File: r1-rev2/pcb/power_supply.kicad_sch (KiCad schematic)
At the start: 25 parts, among them J1 GT-BTP30003-xxxA-16A, Q1 AO3401A, U1 LM66100DCK, U2 TPS62A01DRLR, U3 TPS62A01DRLR, U4 TP4057, U5 XC6206P33xMR

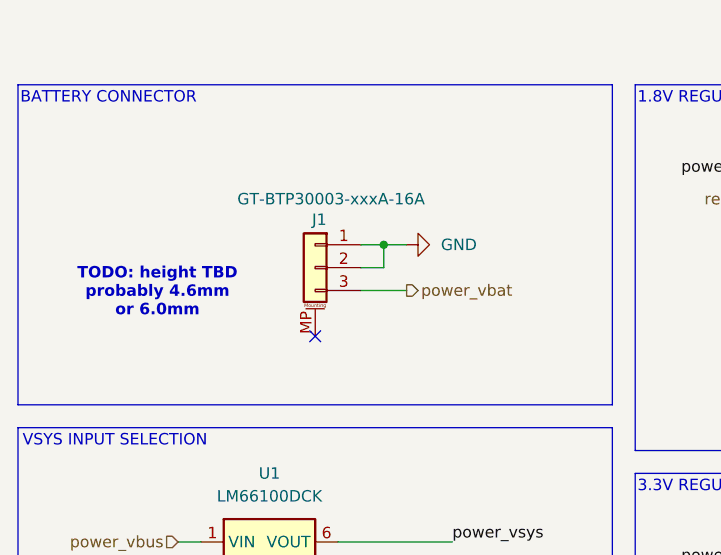
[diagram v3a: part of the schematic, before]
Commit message: R1-Rev2: finish STM32 pin assignment and fix ERC issues
- Expanded LCD bus from 8 to 16 pins so it can be accessed by DMA2D.
- Added RDX pin to LCD bus to allow read access
- Added UART console port for easier access to debug logging
- Shorted USB HS and FS PHYs for DFU mode support
- Connected all GPIOs and peripheral pins
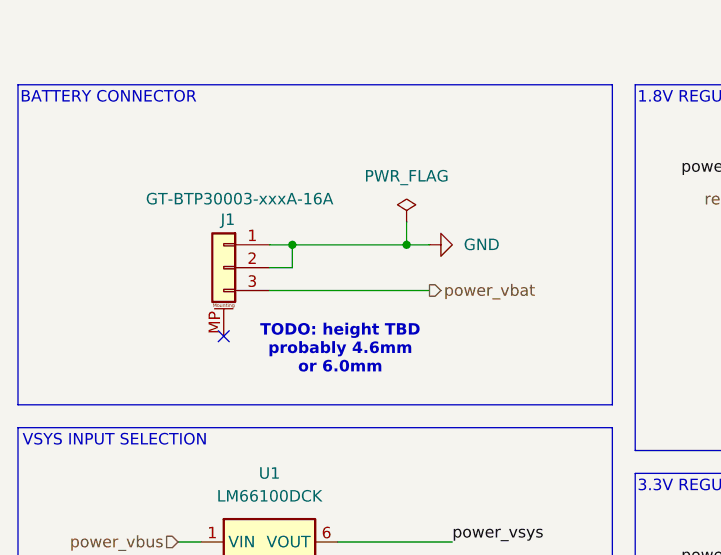
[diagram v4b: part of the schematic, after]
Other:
- moved on the sheet: J1
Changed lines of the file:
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@@
 	(text "TODO: height TBD\nprobably 4.6mm\nor 6.0mm"
 		(exclude_from_sim no)
-		(at 43.434 63.754 0)
+		(at 63.754 70.104 0)
 		(effects
 			(font
@@
 	)
 	(junction
+		(at 71.12 58.42)
+		(diameter 0)
+		(color 0 0 0 0)
+	)
+	(junction
 		(at 147.32 114.3)
 		(diameter 0)
@@
 	)
 	(junction
-		(at 68.58 58.42)
+		(at 58.42 58.42)
 		(diameter 0)
 		(color 0 0 0 0)
@@
 	)
 	(no_connect
-		(at 60.96 68.58)
+		(at 50.8 68.58)
 	)
 	(wire
@@
 	(wire
 		(pts
+			(xy 71.12 55.88) (xy 71.12 58.42)
+		)
+		(stroke
+			(width 0)
+			(type default)
+		)
+	)
+	(wire
+		(pts
 			(xy 129.54 114.3) (xy 129.54 116.84)
 		)
@@
 	(wire
 		(pts
-			(xy 66.04 63.5) (xy 71.12 63.5)
+			(xy 55.88 63.5) (xy 73.66 63.5)
 		)
 		(stroke
@@
 	(wire
 		(pts
-			(xy 66.04 60.96) (xy 68.58 60.96)
+			(xy 55.88 60.96) (xy 58.42 60.96)
 		)
 		(stroke
@@
 	(wire
 		(pts
-			(xy 68.58 58.42) (xy 71.12 58.42)
+			(xy 58.42 58.42) (xy 71.12 58.42)
 		)
 		(stroke
@@
 	(wire
 		(pts
+			(xy 71.12 58.42) (xy 73.66 58.42)
+		)
+		(stroke
+			(width 0)
+			(type default)
+		)
+	)
+	(wire
+		(pts
 			(xy 149.86 60.96) (xy 149.86 63.5)
 		)
@@
 	(wire
 		(pts
-			(xy 66.04 58.42) (xy 68.58 58.42)
+			(xy 55.88 58.42) (xy 58.42 58.42)
 		)
 		(stroke
@@
 	(wire
 		(pts
-			(xy 68.58 58.42) (xy 68.58 60.96)
+			(xy 58.42 58.42) (xy 58.42 60.96)
 		)
 		(stroke
@@
 	(hierarchical_label "power_vbat"
 		(shape output)
-		(at 71.12 63.5 0)
+		(at 73.66 63.5 0)
 		(effects
 			(font
@@
 	(symbol
 		(lib_id "echoplayer:GT-BTP30003")
-		(at 60.96 60.96 0)
+		(at 50.8 60.96 0)
 		(mirror y)
 		(unit 1)
@@
 		(dnp no)
 		(property "Reference" "J1"
-			(at 62.23 55.626 0)
+			(at 52.07 55.626 0)
 			(effects
 				(font
@@
 		)
 		(property "Value" "GT-BTP30003-xxxA-16A"
-			(at 73.152 53.34 0)
+			(at 62.992 53.34 0)
 			(effects
 				(font
@@
 		)
 		(property "Footprint" "echoplayer:Conn_GT-BTP30003-xxxxA-016A"
-			(at 60.96 60.96 0)
+			(at 50.8 60.96 0)
 			(effects
 				(font
@@
 		)
 		(property "Datasheet" "https://www.lcsc.com/datasheet/lcsc_datasheet_2409091552_G-Switch-GT-BTP30003-0460A-016A_C41378737.pdf"
-			(at 60.96 60.96 0)
+			(at 50.8 60.96 0)
 			(effects
 				(font
@@
 		)
 		(property "Description" "3-pin blade/shrapnel battery connector, SMD, vertical mount with mounting pin"
-			(at 60.96 60.96 0)
+			(at 50.8 60.96 0)
 			(effects
 				(font
@@
 	(symbol
 		(lib_id "power:GND")
-		(at 71.12 58.42 90)
+		(at 73.66 58.42 90)
 		(unit 1)
 		(exclude_from_sim no)
@@
 		(fields_autoplaced yes)
 		(property "Reference" "#PWR011"
-			(at 77.47 58.42 0)
+			(at 80.01 58.42 0)
 			(effects
 				(font
@@
 		)
 		(property "Value" "GND"
-			(at 74.93 58.4199 90)
+			(at 77.47 58.4199 90)
 			(effects
 				(font
@@
 		)
 		(property "Footprint" ""
-			(at 71.12 58.42 0)
+			(at 73.66 58.42 0)
 			(effects
 				(font
@@
 		)
 		(property "Datasheet" ""
-			(at 71.12 58.42 0)
+			(at 73.66 58.42 0)
 			(effects
 				(font
@@
 		)
 		(property "Description" "Power symbol creates a global label with name \"GND\" , ground"
-			(at 71.12 58.42 0)
+			(at 73.66 58.42 0)
 			(effects
 				(font
@@
 					(unit 1)
 				)
+			)
+		)
+	)
+	(symbol
+		(lib_id "power:PWR_FLAG")
+		(at 71.12 55.88 0)
+		(unit 1)
+		(exclude_from_sim no)
+		(in_bom yes)
+		(on_board yes)
+		(dnp no)
+		(fields_autoplaced yes)
+		(property "Reference" "#FLG010"
+			(at 71.12 53.975 0)
+			(effects
+				(font
+					(size 1.27 1.27)
+				)
+				(hide yes)
+			)
+		)
+		(property "Value" "PWR_FLAG"
+			(at 71.12 50.8 0)
+			(effects
+				(font
+					(size 1.27 1.27)
+				)
+			)
+		)
+		(property "Footprint" ""
+			(at 71.12 55.88 0)
+			(effects
+				(font
+					(size 1.27 1.27)
+				)
+				(hide yes)
+			)
+		)
+		(property "Datasheet" "~"
+			(at 71.12 55.88 0)
+			(effects
+				(font
+					(size 1.27 1.27)
+				)
+				(hide yes)
+			)
+		)
+		(property "Description" "Special symbol for telling ERC where power comes from"
+			(at 71.12 55.88 0)
+			(effects
+				(font
+					(size 1.27 1.27)
+				)
+				(hide yes)
+			)
+		)
+		(pin "1"
+		)
+		(instances
+			(project "echo-r1"
+				(path "/aa241847-30f4-429d-a148-6a6e39ba98e0/48d39f5c-11a4-46cd-927a-56a9c6ae42fa"
+					(reference "#FLG010")
+					(unit 1)
+				)

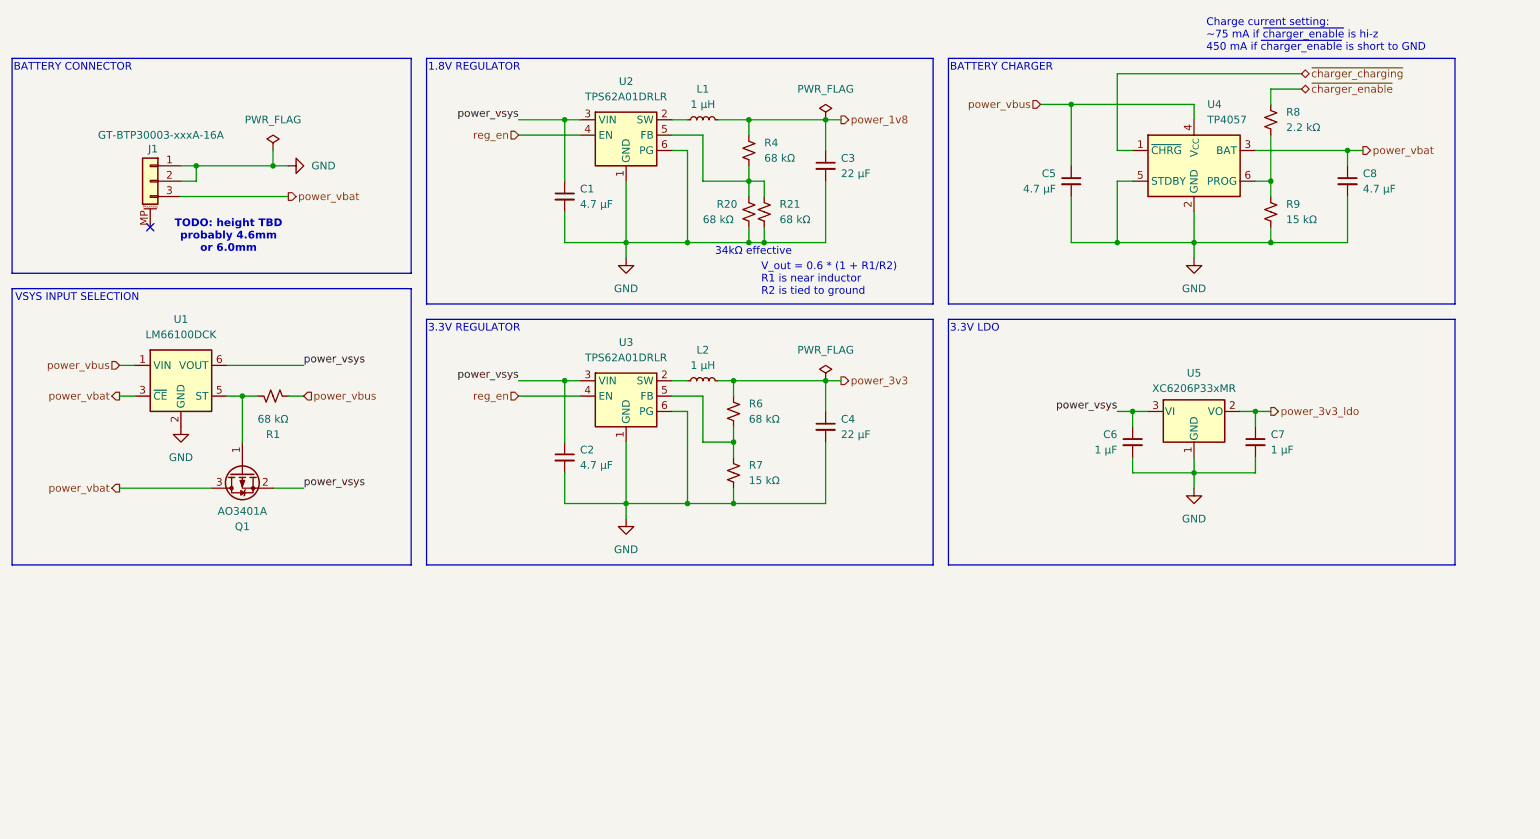
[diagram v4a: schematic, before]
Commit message: R1-Rev2: update LDO power supplies for codec and RTC
The codec analog supplies (AVDD/DRVDD) are now fed through
a 3.0V LDO powered off the main 3.3V buck regulator, which
improves worst case efficiency from ~78% to around 86% and
avoids stability issues that might occur when the battery
gets within the dropout voltage range.

The new LDO (AP2125) has a very low dropout at loads well
above what the codec draws, so it should function perfectly
even at low battery levels. In theory, everything except
the memory card should still function almost all the way
down to 3.0V.

A second LDO powered from the battery is still needed just
for the RTC, but that's not too big a deal.
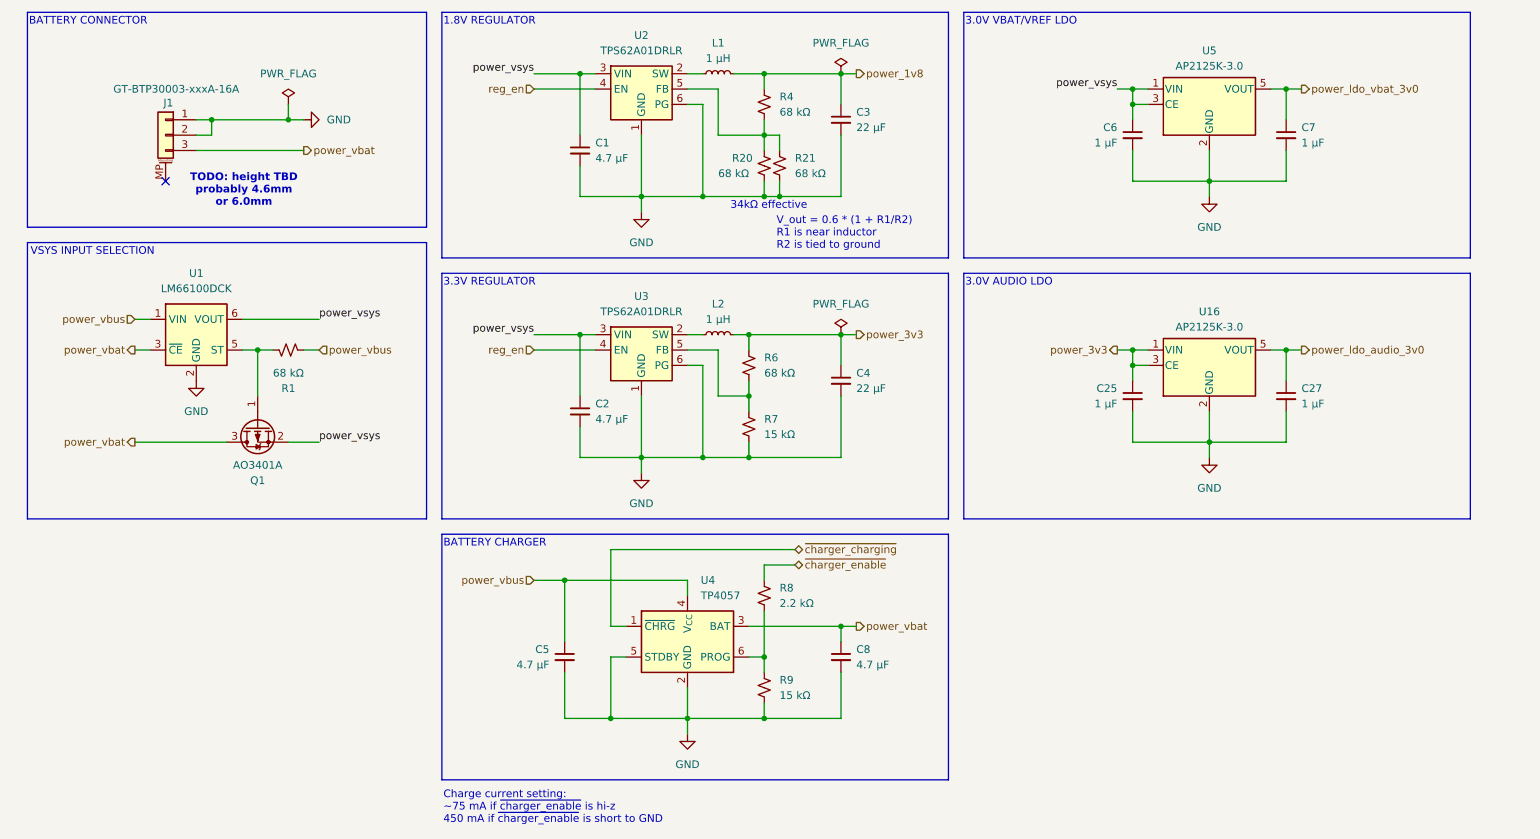
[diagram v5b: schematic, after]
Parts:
- removed U5: XC6206P33xMR, Package_TO_SOT_SMD:SOT-23-3, symbol Regulator_Linear:XC6206PxxxMR
- added C25, C27: 1 µF, Capacitor_SMD:C_0402_1005Metric, symbol Device:C_Small
- added U16, U5: AP2125K-3.0, Package_TO_SOT_SMD:SOT-23-5, symbol echoplayer:AP2125K-3.0
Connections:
- net GND: now also C25.2, C27.2, U16.2 (GND), U16.4 (NC), U5.2 (GND), U5.4 (NC)
- net power_3v3: now also C25.1, U16.1 (VIN), U16.3 (CE)
- net power_vsys: now also U5.1 (VIN), U5.3 (CE)
- net power_3v3_ldo renamed power_ldo_vbat_3v0
- net power_ldo_vbat_3v0: now also U5.5 (VOUT)
- new net power_ldo_audio_3v0: C27.1, U16.5 (VOUT)
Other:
- note added: "3.0V AUDIO LDO"
- note added: "3.0V VBAT/VREF LDO"
- note removed: "3.3V LDO"
- moved on the sheet: C1, C2, C3, C4, C5, C6, C7, C8, J1, L1, L2, Q1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

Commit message: R1-Rev2: updates to PCB layout, add HyperRAM routing
- Reannotate schematic and assign footprints for passives
- First try at HyperRAM routing
- Fixed incorrect W958D8NBYA5I pinout
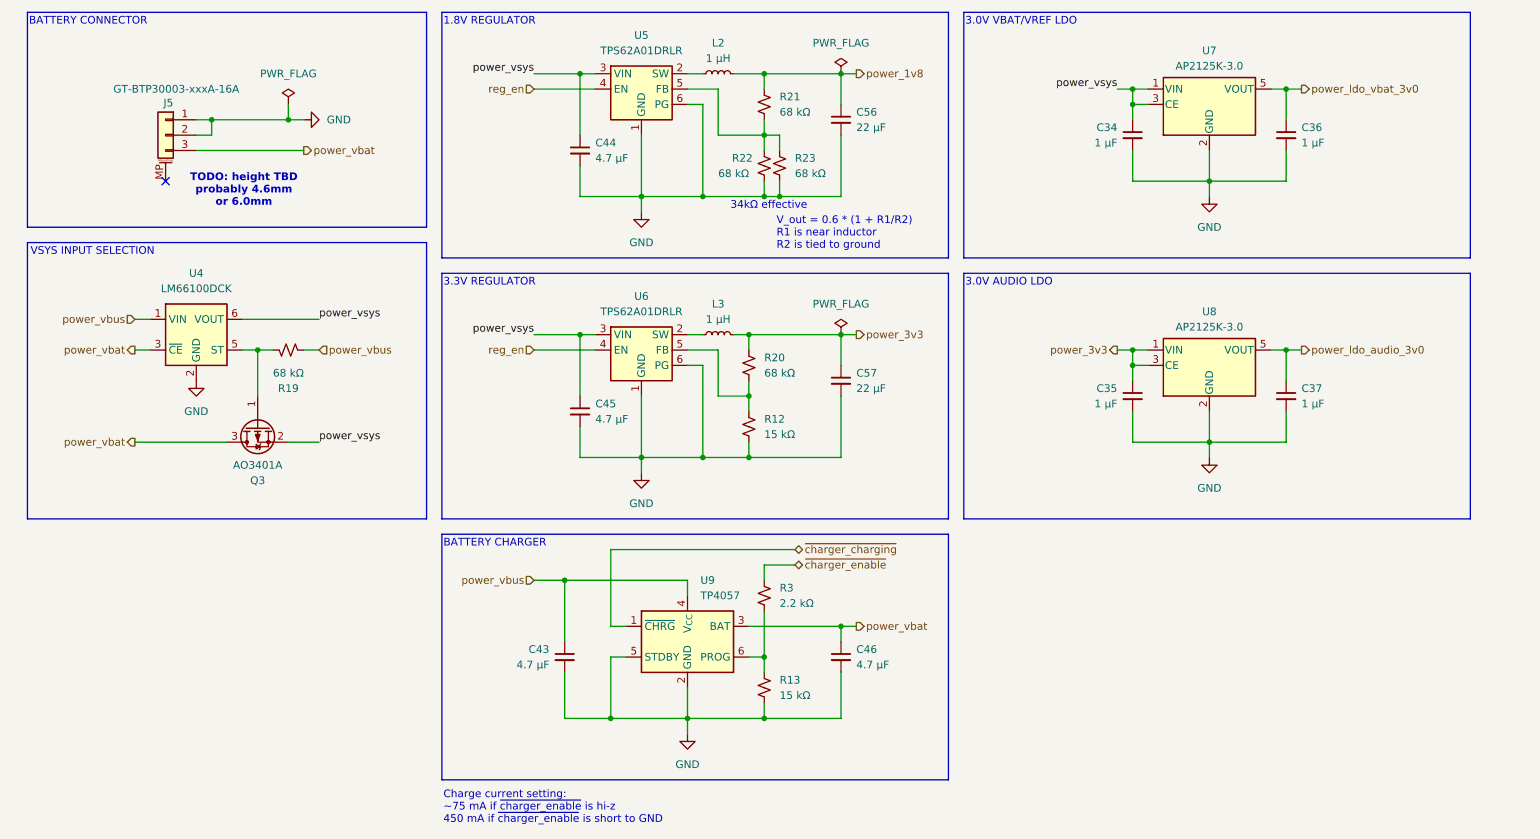
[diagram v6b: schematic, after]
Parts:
- C43: renamed from C5; footprint Capacitor_SMD:C_0603_1608Metric -> Capacitor_SMD:C_0805_2012Metric
- C46: renamed from C8; footprint Capacitor_SMD:C_0603_1608Metric -> Capacitor_SMD:C_0805_2012Metric
- L2: renamed from L1; footprint echoplayer:L_0806_2016Metric -> (none)
- L3: renamed from L2; footprint echoplayer:L_0806_2016Metric -> (none)
- R12: renamed from R7; footprint Resistor_SMD:R_0603_1608Metric -> Resistor_SMD:R_0402_1005Metric
- R20: renamed from R6; footprint Resistor_SMD:R_0603_1608Metric -> Resistor_SMD:R_0402_1005Metric
- R21: renamed from R4; footprint Resistor_SMD:R_0603_1608Metric -> Resistor_SMD:R_0402_1005Metric
- R22: renamed from R20; footprint Resistor_SMD:R_0603_1608Metric -> Resistor_SMD:R_0402_1005Metric
- R23: renamed from R21; footprint Resistor_SMD:R_0603_1608Metric -> Resistor_SMD:R_0402_1005Metric
- renumbered C6 to C34, C25 to C35, C7 to C36, C27 to C37, C1 to C44, C2 to C45, C3 to C56, C4 to C57, J1 to J5, Q1 to Q3, R9 to R13, R1 to R19, R8 to R3, U1 to U4, U2 to U5, U3 to U6, U5 to U7, U16 to U8, U4 to U9

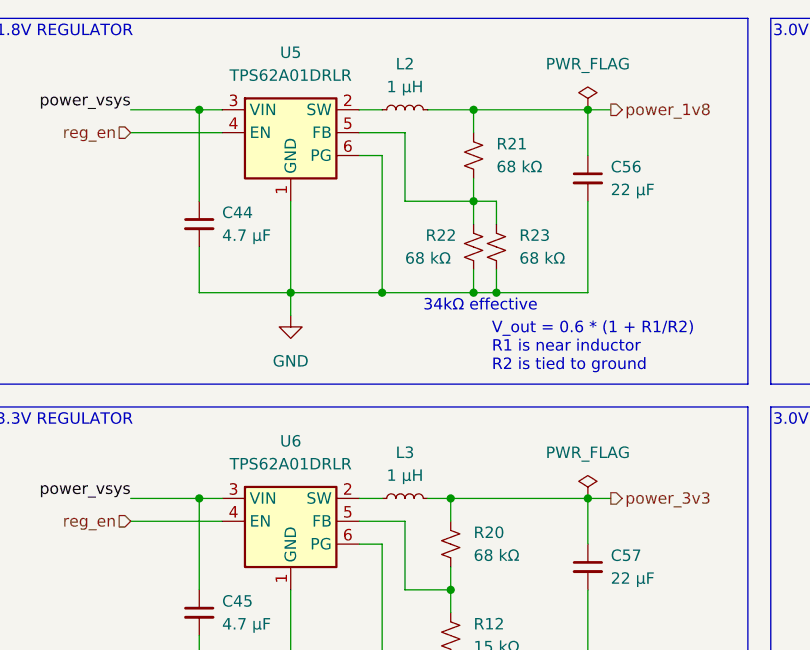
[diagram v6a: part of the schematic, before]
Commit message: R1-Rev2: add inductor footprint and group components
Also use the same 2.2uH inductor for the buck converters,
to minimize unique component count.
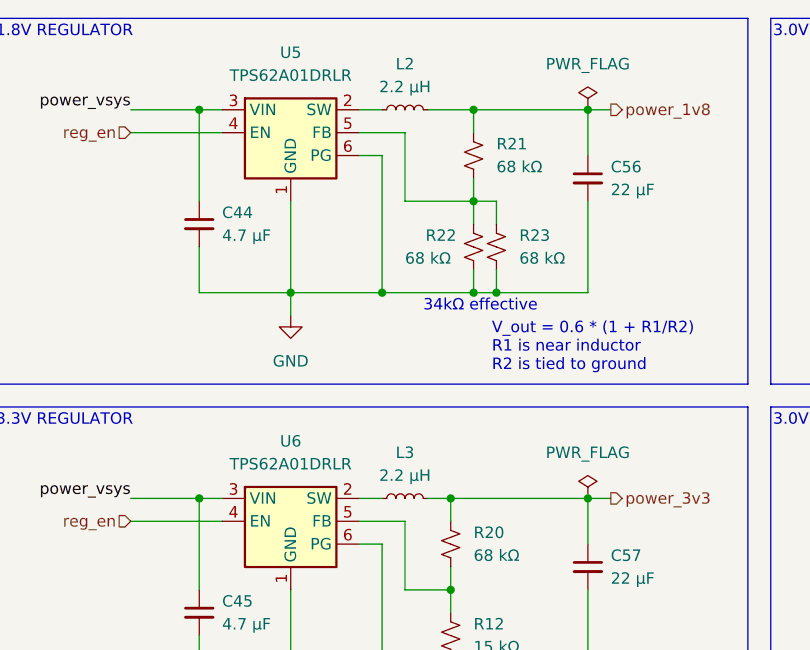
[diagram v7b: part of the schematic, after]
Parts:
- L2, L3: value 1 µH -> 2.2 µH; footprint (none) -> Inductor_SMD:L_Changjiang_FNR3015S
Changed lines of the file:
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@@
 			)
 		)
-		(property "Value" "1 µH"
+		(property "Value" "2.2 µH"
 			(at 144.78 83.82 90)
 			(effects
@@
 			)
 		)
-		(property "Footprint" ""
+		(property "Footprint" "Inductor_SMD:L_Changjiang_FNR3015S"
 			(at 144.78 86.36 0)
 			(effects
@@
 			)
 		)
-		(property "Value" "1 µH"
+		(property "Value" "2.2 µH"
 			(at 144.78 40.64 90)
 			(effects
@@
 			)
 		)
-		(property "Footprint" ""
+		(property "Footprint" "Inductor_SMD:L_Changjiang_FNR3015S"
 			(at 144.78 43.18 0)
 			(effects
